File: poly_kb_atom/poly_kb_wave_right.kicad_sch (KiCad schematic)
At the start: 66 parts, among them J37 0.96" Display, J38 Conn_01x06, J39 Conn_01x03, J40 Conn_01x03_Male, J43 FPC-05F-12PH15, J44 Conn_01x05, SW1 RotaryEncoder_Switch, U2 TD6811, U3 MT9700

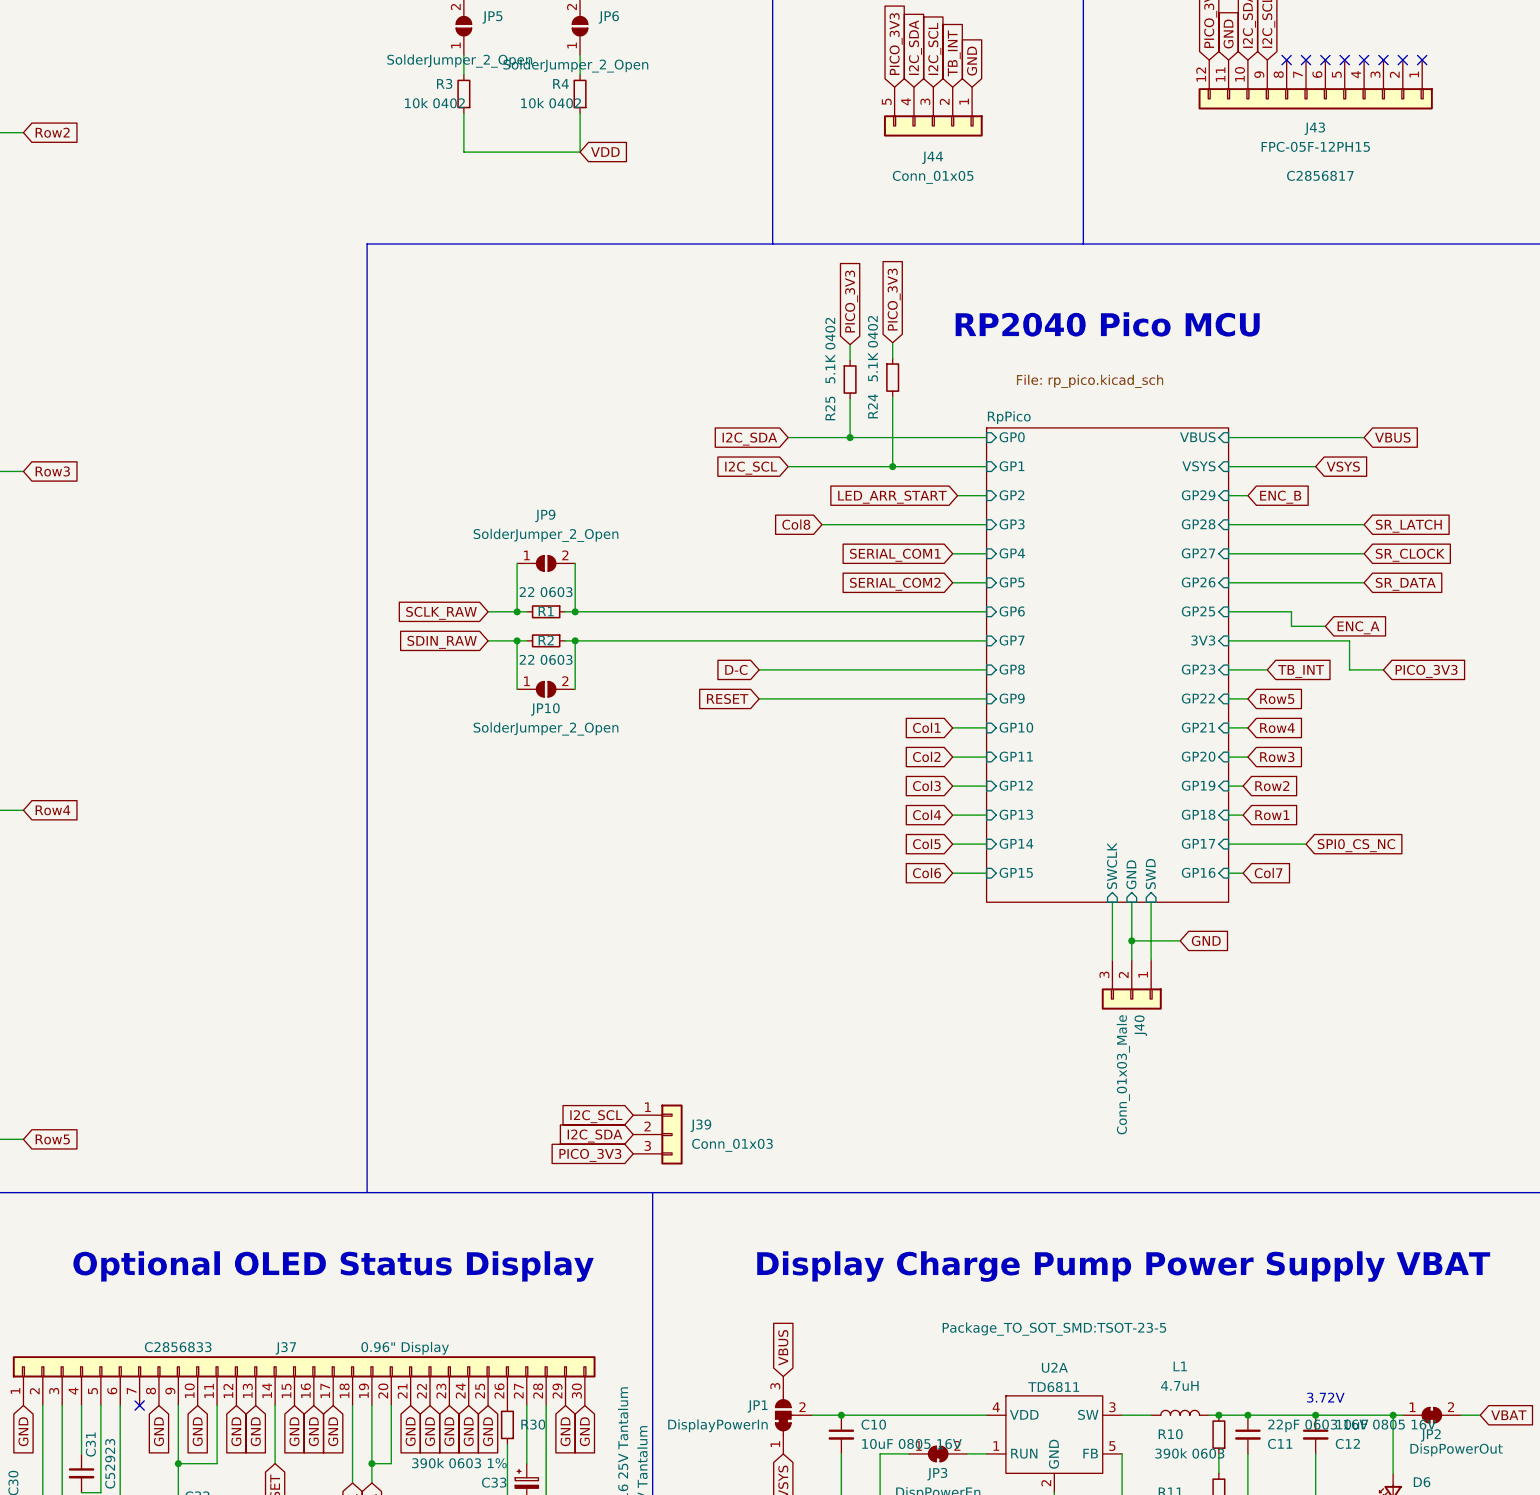
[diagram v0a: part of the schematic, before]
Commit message: QFN shift register version
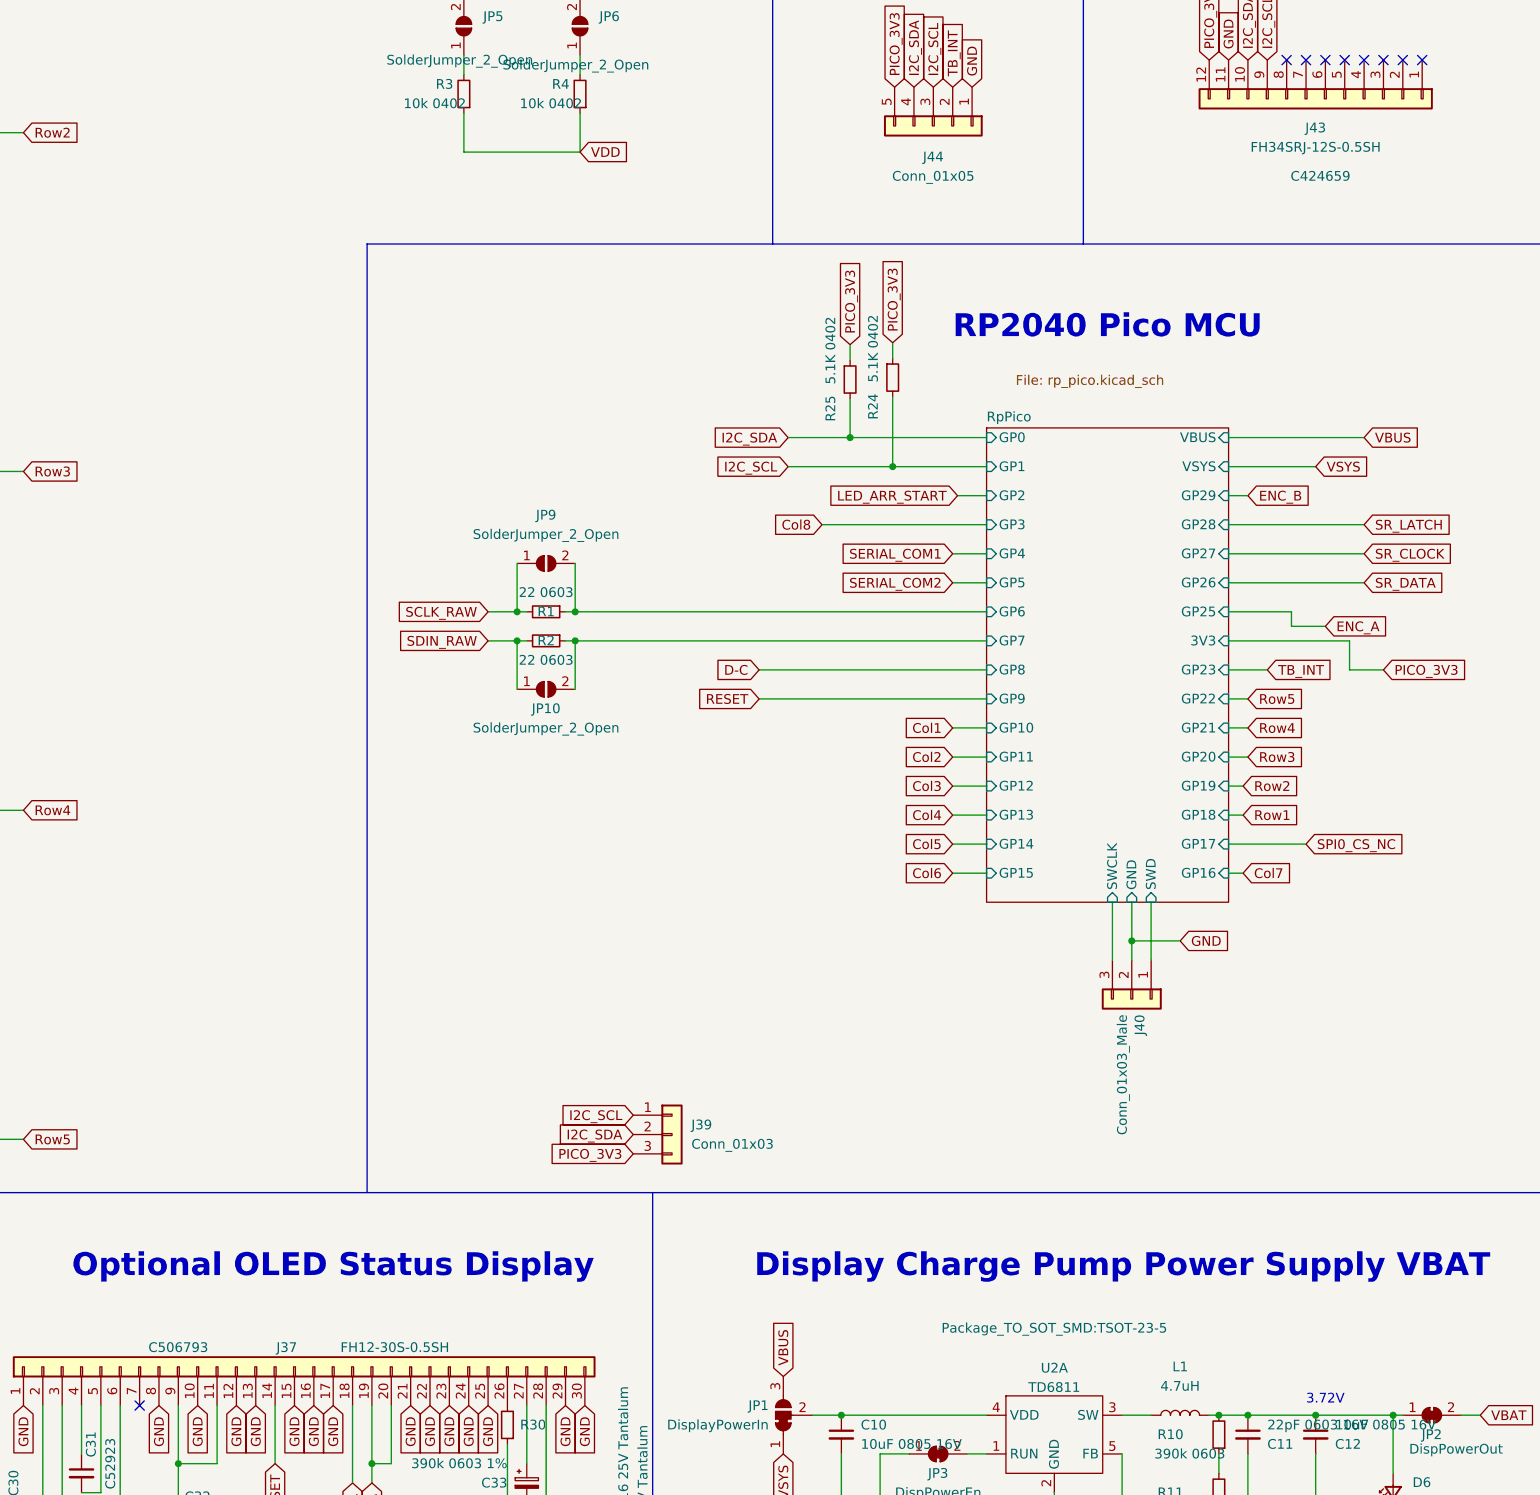
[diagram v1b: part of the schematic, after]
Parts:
- J37: value 0.96" Display -> FH12-30S-0.5SH; footprint poly_kb:XUNPU-FPC-05FB-30PH20 -> Connector_FFC-FPC:Hirose_FH12-30S-0.5SH_1x30-1MP_P0.50mm_Horizontal; LCSC C2856833 -> C506793; MPN FPC-05FB-30PH20 -> FH12-30S-0.5SH
- J43: value FPC-05F-12PH15 -> FH34SRJ-12S-0.5SH; footprint poly_kb:XUNPU-FPC-05F-12PH15 -> poly_kb:FH34SRJ12S05SH50; LCSC C2856817 -> C424659; MPN FPC-05F-12PH15 -> FH34SRJ-12S-0.5SH
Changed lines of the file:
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@@
       (effects (font (size 1.27 1.27)) (justify left))
     )
-    (property "Value" "0.96\" Display" (id 1) (at 434.34 289.56 90)
+    (property "Value" "FH12-30S-0.5SH" (id 1) (at 434.34 289.56 90)
       (effects (font (size 1.27 1.27)) (justify left))
     )
-    (property "Footprint" "poly_kb:XUNPU-FPC-05FB-30PH20" (id 2) (at 414.02 292.1 0)
+    (property "Footprint" "Connector_FFC-FPC:Hirose_FH12-30S-0.5SH_1x30-1MP_P0.50mm_Horizontal" (id 2) (at 414.02 292.1 0)
       (effects (font (size 1.27 1.27)) hide)
     )
-    (property "Datasheet" "https://datasheet.lcsc.com/lcsc/2109221030_XUNPU-FPC-05FB-30PH20_C2856833.pdf" (id 3) (at 414.02 292.1 0)
+    (property "Datasheet" "https://datasheet.lcsc.com/lcsc/2004261434_HRS-Hirose-FH12-30S-0-5SH-55_C506793.pdf" (id 3) (at 414.02 292.1 0)
       (effects (font (size 1.27 1.27)) hide)
     )
-    (property "LCSC" "C2856833" (id 4) (at 398.78 289.56 90))
-    (property "MPN" "FPC-05FB-30PH20" (id 5) (at 414.02 292.1 0)
+    (property "LCSC" "C506793" (id 4) (at 398.78 289.56 90))
+    (property "MPN" "FH12-30S-0.5SH" (id 5) (at 414.02 292.1 0)
       (effects (font (size 1.27 1.27)) hide)
     )
@@
     (in_bom yes) (on_board yes)
     (property "Reference" "J43" (id 0) (at 548.005 129.54 90))
-    (property "Value" "FPC-05F-12PH15" (id 1) (at 548.005 132.08 90))
-    (property "Footprint" "poly_kb:XUNPU-FPC-05F-12PH15" (id 2) (at 549.275 125.73 0)
+    (property "Value" "FH34SRJ-12S-0.5SH" (id 1) (at 548.005 132.08 90))
+    (property "Footprint" "poly_kb:FH34SRJ12S05SH50" (id 2) (at 549.275 125.73 0)
       (effects (font (size 1.27 1.27)) hide)
     )
-    (property "Datasheet" "https://datasheet.lcsc.com/lcsc/2109221030_XUNPU-FPC-05F-12PH15_C2856817.pdf" (id 3) (at 563.88 141.605 90)
+    (property "Datasheet" "https://datasheet.lcsc.com/lcsc/1912111437_HRS-Hirose-FH34SRJ-12S-0-5SH-50_C424659.pdf" (id 3) (at 563.88 141.605 90)
       (effects (font (size 1.27 1.27)) hide)
     )
-    (property "LCSC" "C2856817" (id 4) (at 548.64 135.89 90))
-    (property "MPN" "FPC-05F-12PH15" (id 5) (at 549.275 125.73 0)
+    (property "LCSC" "C424659" (id 4) (at 548.64 135.89 90))
+    (property "MPN" "FH34SRJ-12S-0.5SH" (id 5) (at 549.275 125.73 0)
       (effects (font (size 1.27 1.27)) hide)
     )
@@
     )
     (path "/3e33f9c9-0497-46b7-bb2b-d0232f017745"
-      (reference "J37") (unit 1) (value "0.96\" Display") (footprint "poly_kb:XUNPU-FPC-05FB-30PH20")
+      (reference "J37") (unit 1) (value "FH12-30S-0.5SH") (footprint "Connector_FFC-FPC:Hirose_FH12-30S-0.5SH_1x30-1MP_P0.50mm_Horizontal")
     )
     (path "/6a7d08be-e394-4ca2-a475-c05057a256f5"
@@
     )
     (path "/99d83d11-b838-453d-a021-daa0ba821a8f"
-      (reference "J43") (unit 1) (value "FPC-05F-12PH15") (footprint "poly_kb:XUNPU-FPC-05F-12PH15")
+      (reference "J43") (unit 1) (value "FH34SRJ-12S-0.5SH") (footprint "poly_kb:FH34SRJ12S05SH50")
     )
     (path "/d2c2da56-8f2d-4b5e-bdab-e02a92608447"
@@
       (reference "U3") (unit 1) (value "MT9700") (footprint "Package_TO_SOT_SMD:SOT-23-5")
     )
-    (path "/92e782d8-f8e0-4b6b-8c13-c5574675ce33/a48221cf-2c41-4b92-8677-536dfa81d722"
-      (reference "U4") (unit 1) (value "74HCT595") (footprint "Package_SO:SOIC-16_3.9x9.9mm_P1.27mm")
+    (path "/92e782d8-f8e0-4b6b-8c13-c5574675ce33/a7dea223-23f1-4108-a620-c973c7725973"
+      (reference "U4") (unit 1) (value "74HCT595") (footprint "SOT:SOT-763-1")
     )
-    (path "/92e782d8-f8e0-4b6b-8c13-c5574675ce33/6d5e0d83-8232-40cc-acdb-aa7c18220b7b"
-      (reference "U5") (unit 1) (value "74HCT595") (footprint "Package_SO:SOIC-16_3.9x9.9mm_P1.27mm")
+    (path "/92e782d8-f8e0-4b6b-8c13-c5574675ce33/90e40116-b077-4d7e-9bb4-b9a608e83642"
+      (reference "U5") (unit 1) (value "74HCT595") (footprint "SOT:SOT-763-1")
     )
-    (path "/92e782d8-f8e0-4b6b-8c13-c5574675ce33/5b298751-6c02-40fa-a24c-f545ec632e4e"
-      (reference "U6") (unit 1) (value "74HCT595") (footprint "Package_SO:SOIC-16_3.9x9.9mm_P1.27mm")
+    (path "/92e782d8-f8e0-4b6b-8c13-c5574675ce33/3f5e21a9-9ac1-47b2-b0a7-cf9edd604f97"
+      (reference "U6") (unit 1) (value "74HCT595") (footprint "SOT:SOT-763-1")
     )
-    (path "/92e782d8-f8e0-4b6b-8c13-c5574675ce33/f4234d4d-0685-42ef-9578-91c9044cf481"
-      (reference "U7") (unit 1) (value "74HCT595") (footprint "Package_SO:SOIC-16_3.9x9.9mm_P1.27mm")
+    (path "/92e782d8-f8e0-4b6b-8c13-c5574675ce33/90775456-d44d-426e-9f55-64e847e26563"
+      (reference "U7") (unit 1) (value "74HCT595") (footprint "SOT:SOT-763-1")
     )
     (path "/92e782d8-f8e0-4b6b-8c13-c5574675ce33/578e1d72-8ef4-4ac0-b24c-23843feed8de"
-      (reference "U8") (unit 1) (value "74HCT595") (footprint "Package_SO:SOIC-16_3.9x9.9mm_P1.27mm")
+      (reference "U8") (unit 1) (value "74HCT595") (footprint "SOT:SOT-763-1")
     )
     (path "/5b575f2a-a831-41f0-985e-3d214d07238c/e269b6e6-9935-4c4d-adf7-697611ddd102"

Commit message: Current production version of right side and added STLs
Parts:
- C1, C2: LCSC C1634 -> (none); MPN CL10C100JB8NNNC -> C1634
- C10, C12, C13, C14: LCSC C15850 -> (none); MPN CL21A106KAYNNNE -> C15850
- C11: LCSC C1653 -> (none); MPN CL10C220JB8NNNC -> C1653
- C30, C31, C32: LCSC C52923 -> (none); MPN CL05A105KA5NQNC -> C52923
- C33, C34: value 4.7uF 3216 25V Tantalum -> CA45-A-25V-4.7uF-K 4.7uF 3216 25V Tantalum; LCSC C129569 -> (none); MPN CA45-A-25V-4.7uF-K -> C129569
- D12: LCSC C2128 -> (none); MPN 1N4148WS -> C2128
- D5: value Blue 0805 -> Green 0805; LCSC C2293 -> (none); MPN (none) -> C2297
- D6: LCSC C2296 -> (none); MPN (none) -> C2296
- J37: LCSC C506793 -> (none); MPN FH12-30S-0.5SH -> C506793
- J40: LCSC (none) -> (none); MPN (none) -> (none)
- J43: LCSC C424659 -> (none); MPN FH34SRJ-12S-0.5SH -> C424659
- L1: LCSC C2836880 -> (none); MPN MCS0530-4R7MN2 -> C2836880
- R1, R2: LCSC C23345 -> (none); MPN (none) -> C23345
- R10, R11: LCSC C25908 -> (none); MPN (none) -> C23150
- R12: LCSC C22807 -> (none); MPN (none) -> C22807
- R13: LCSC C31850 -> (none); MPN (none) -> C31850
- R24, R25: LCSC C25905 -> (none); MPN (none) -> C25905
- R3, R4: value 10k 0402 -> 10k 0603; LCSC C23162 -> (none); MPN (none) -> C25804
- R30: LCSC C23150 -> (none); MPN (none) -> C23150
- R5, R6: LCSC C21190 -> (none); MPN (none) -> C21190
- U2: LCSC C189486 -> (none); MPN TD6811 -> C189486
- U3: LCSC C89855 -> (none); MPN MT9700 -> C89855
- USB2: LCSC C165948 -> (none); MPN TYPE-C-31-M-12 -> C165948
